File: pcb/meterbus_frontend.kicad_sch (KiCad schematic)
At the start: 34 parts, among them Q1 2N7002, U1 78L05G, U3 ISO6721RBDR, U5 74HC14D

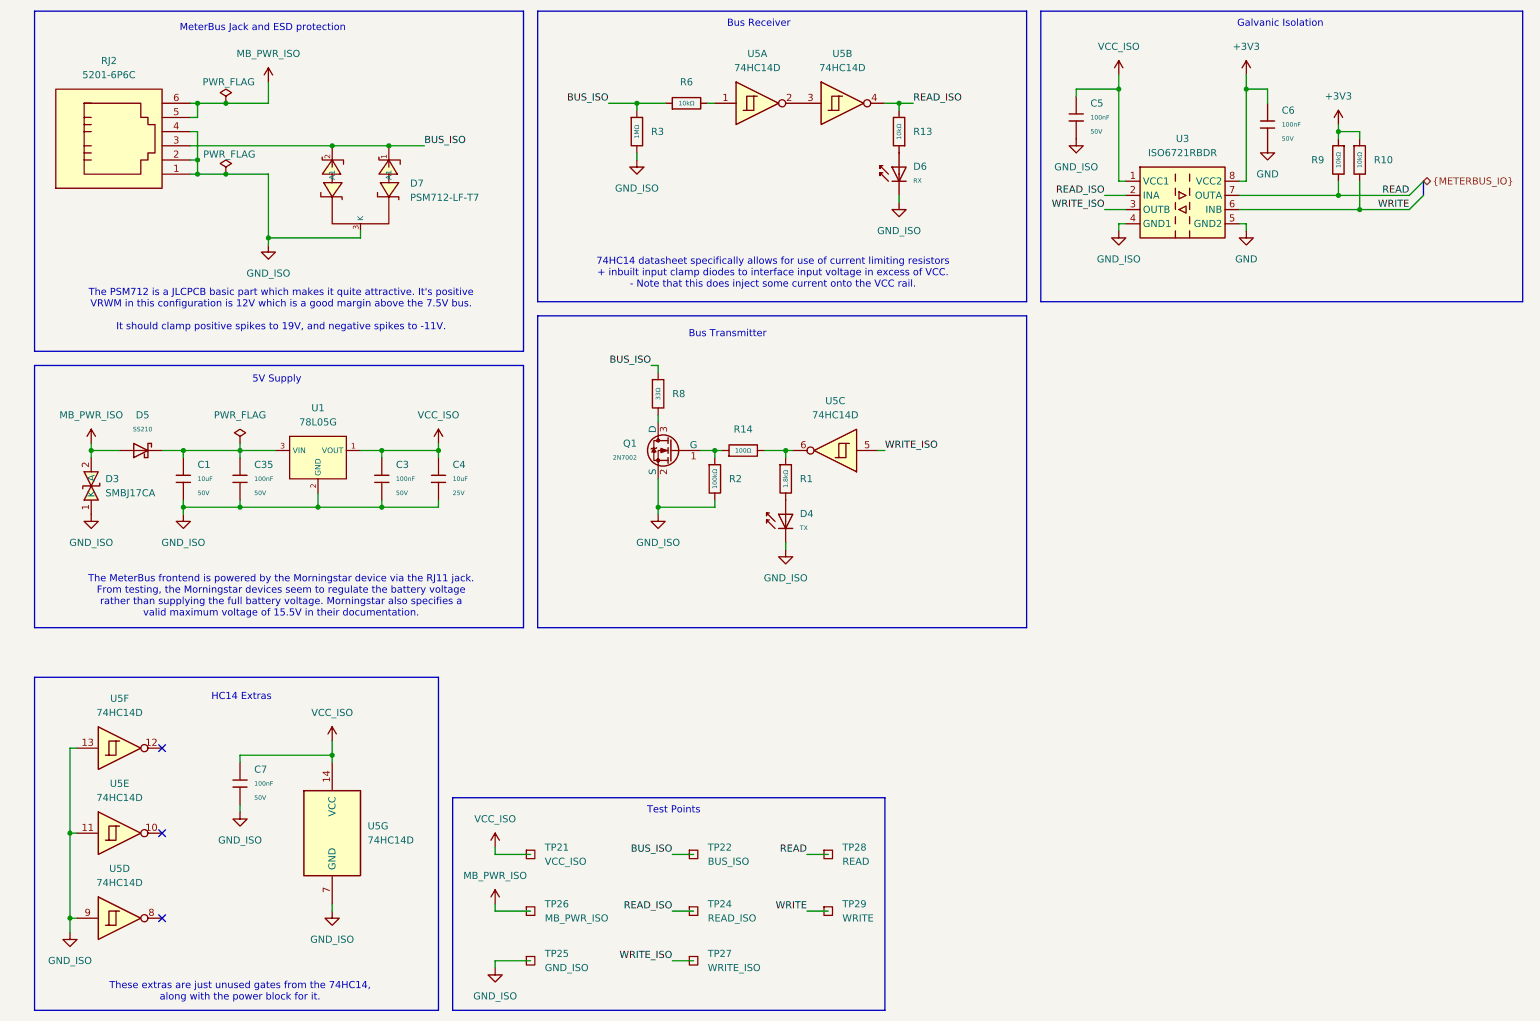
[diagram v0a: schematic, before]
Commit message: pcb: layout and route meterbus frontend
Places parts PCB traces for MeterBus frontend.
Also changes which gates on HC14 schematic are used to simplify routing.
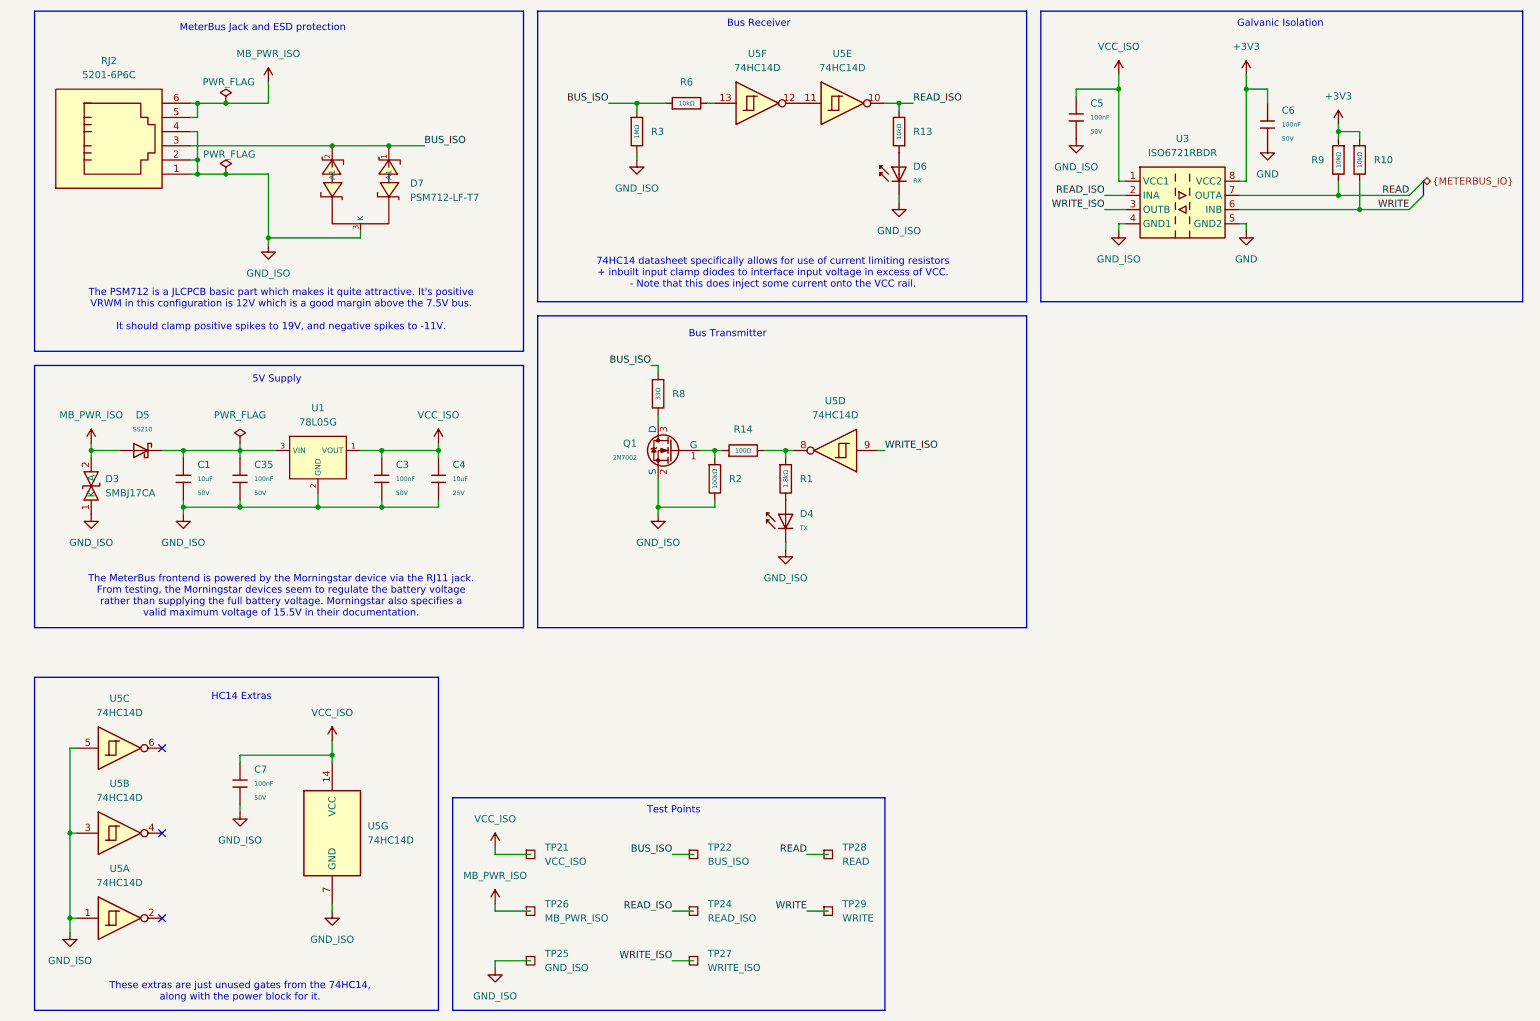
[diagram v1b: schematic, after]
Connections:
- net GND_ISO: now also U5.1, U5.3, U5.5; no longer U5.11, U5.13, U5.9
- net READ_ISO: now also U5.10; no longer U5.4
- net WRITE_ISO: now also U5.9; no longer U5.5
- net at R1.1, R14.2: now also U5.8; no longer U5.6
- net at R6.2: now also U5.13; no longer U5.1
- net at U5.2: no longer U5.3
- net at U5.12: now also U5.11
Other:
- moved on the sheet: U5A, U5B, U5C, U5D, U5E, U5F

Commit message: pcb: adjust drc rules to match jlc
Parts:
- TP22: value BUS_ISO -> BUS
- TP24: value READ_ISO -> RX_ISO
- TP26: value MB_PWR_ISO -> BAT_ISO
- TP27: value WRITE_ISO -> TX_ISO
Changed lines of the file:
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@@
 			)
 		)
-		(property "Value" "MB_PWR_ISO"
+		(property "Value" "BAT_ISO"
 			(at 106.68 177.7999 0)
 			(show_name no)
@@
 			)
 		)
-		(property "Value" "READ_ISO"
+		(property "Value" "RX_ISO"
 			(at 135.89 177.7999 0)
 			(show_name no)
@@
 			)
 		)
-		(property "Value" "WRITE_ISO"
+		(property "Value" "TX_ISO"
 			(at 135.89 186.6899 0)
 			(show_name no)
@@
 			)
 		)
-		(property "Value" "BUS_ISO"
+		(property "Value" "BUS"
 			(at 135.89 167.6399 0)
 			(show_name no)
